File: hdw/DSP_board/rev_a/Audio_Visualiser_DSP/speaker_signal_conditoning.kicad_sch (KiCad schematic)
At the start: 6 parts, among them J1401 Left, T1401 Transformer_Audio

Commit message: assigned some footprints
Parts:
- R1401, R1402: footprint (none) -> Resistors_SMD:R_0805
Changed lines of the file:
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@@
 			)
 		)
-		(property "Footprint" ""
+		(property "Footprint" "Resistors_SMD:R_0805"
 			(at 132.08 63.5 0)
 			(hide yes)
@@
 				(font
 					(size 1.524 1.524)
+				)
+			)
+		)
+		(property "Sim.Type" ""
+			(at 132.08 63.5 90)
+			(hide yes)
+			(show_name no)
+			(do_not_autoplace no)
+			(effects
+				(font
+					(size 1.27 1.27)
 				)
 			)
@@
 			)
 		)
+		(property "Sim.Type" ""
+			(at 119.38 63.5 90)
+			(hide yes)
+			(show_name no)
+			(do_not_autoplace no)
+			(effects
+				(font
+					(size 1.27 1.27)
+				)
+			)
+		)
 		(pin "2"
 		)
@@
 			)
 		)
+		(property "Sim.Type" ""
+			(at 179.07 63.5 90)
+			(hide yes)
+			(show_name no)
+			(do_not_autoplace no)
+			(effects
+				(font
+					(size 1.27 1.27)
+				)
+			)
+		)
 		(pin "2"
 		)
@@
 			)
 		)
-		(property "Footprint" ""
+		(property "Footprint" "Resistors_SMD:R_0805"
 			(at 140.97 57.15 0)
 			(hide yes)
@@
 		)
 		(property "Digi-Key PN" ""
+			(at 140.97 57.15 0)
+			(hide yes)
+			(show_name no)
+			(do_not_autoplace no)
+			(effects
+				(font
+					(size 1.27 1.27)
+				)
+			)
+		)
+		(property "Sim.Type" ""
 			(at 140.97 57.15 0)
 			(hide yes)
@@
 		)
 		(property "Description" "Audio transformer"
+			(at 87.63 68.58 0)
+			(hide yes)
+			(show_name no)
+			(do_not_autoplace no)
+			(effects
+				(font
+					(size 1.27 1.27)
+				)
+			)
+		)
+		(property "Sim.Type" ""
 			(at 87.63 68.58 0)
 			(hide yes)
@@
 			(at 59.69 67.31 0)
 			(hide yes)
+			(show_name no)
+			(do_not_autoplace no)
+			(effects
+				(font
+					(size 1.27 1.27)
+				)
+			)
+		)
+		(property "Sim.Type" ""
+			(at 59.69 67.31 0)
+			(hide yes)

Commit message: assigned many digi-key part numbers
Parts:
- removed C1401: 2.2uF, Capacitors_SMD:C_0402, symbol Custom Library:C_Custom
- removed J1401: Left, symbol Connector:Screw_Terminal_01x02
- removed T1401: Transformer_Audio, symbol Device:Transformer_Audio
- D1401: Digi-Key PN (none) -> BAT54SWT1GOSCT-ND
- R1401, R1402: Digi-Key PN (none) -> 311-20.0KCRCT-ND; Wattage 1/4W -> 1/8W

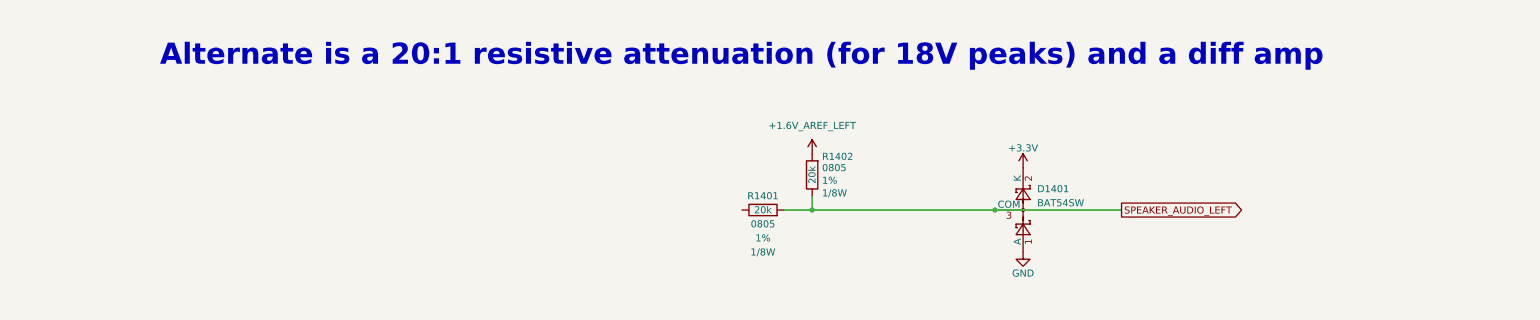
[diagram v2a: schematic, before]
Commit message: started speaker signal conditioning
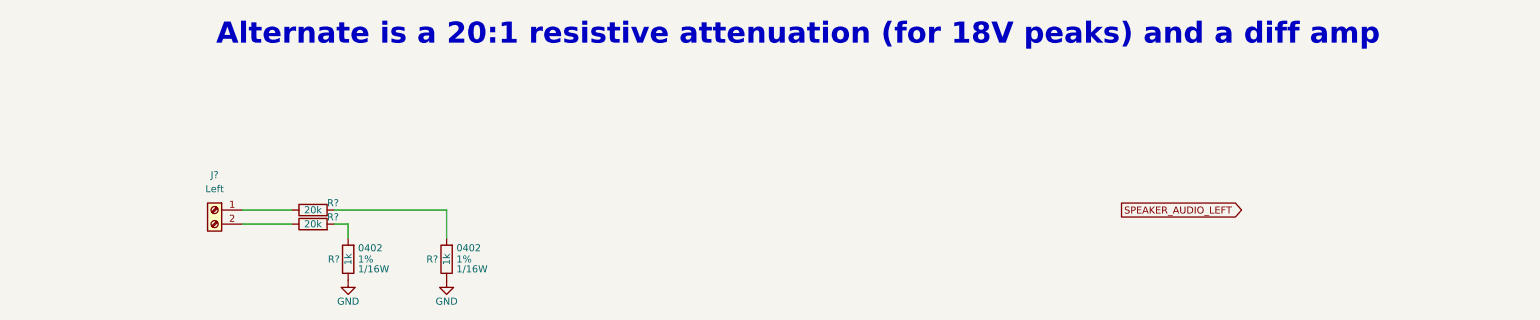
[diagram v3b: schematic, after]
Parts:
- removed D1401: BAT54SW, Package_TO_SOT_SMD:SOT-323_SC-70, symbol Diode:BAT54SW
- removed R1401: 20k, Resistors_SMD:R_0805, symbol Custom Library:R_Custom
- removed R1402: 20k, Resistors_SMD:R_0805, symbol Custom_Library:R_Custom
- added J?: Left, TerminalBlock_Phoenix:TerminalBlock_Phoenix_MKDS-1,5-2-5.08_1x02_P5.08mm_Horizontal, symbol Connector:Screw_Terminal_01x02
- added R? (x2): 1k, Resistors_SMD:R_0402, symbol Custom_Library:R_Custom
- added R? (x2): 20k, Resistors_SMD:R_0402, symbol Custom Library:R_Custom
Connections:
- net GND: now also R?.2, R?.2
- new net: R?.1, R?.1 (x2)
- new net: J?.1 (Pin_1), R?.2
- new net: J?.2 (Pin_2), R?.2

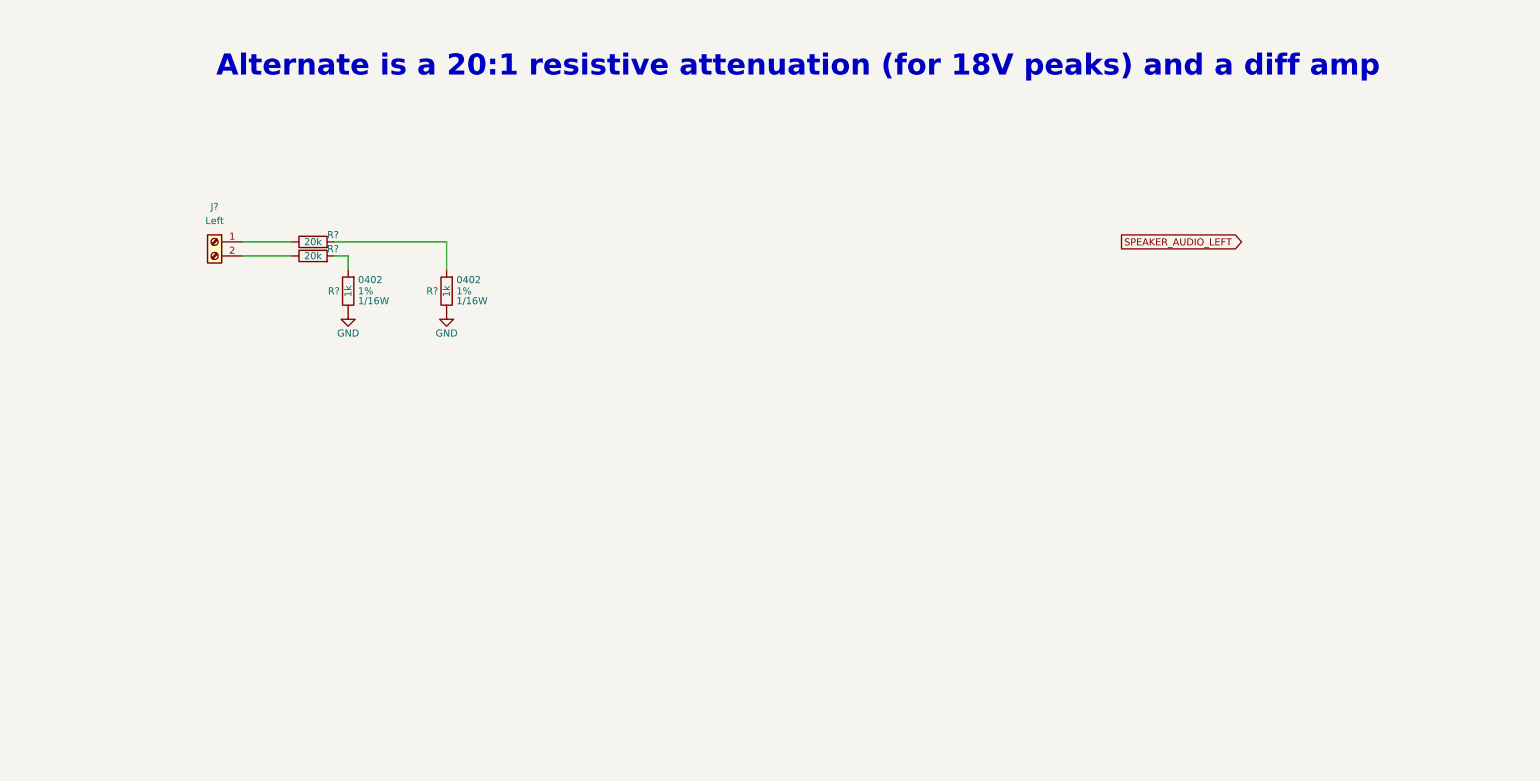
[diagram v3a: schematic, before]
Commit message: Added speaker signal path
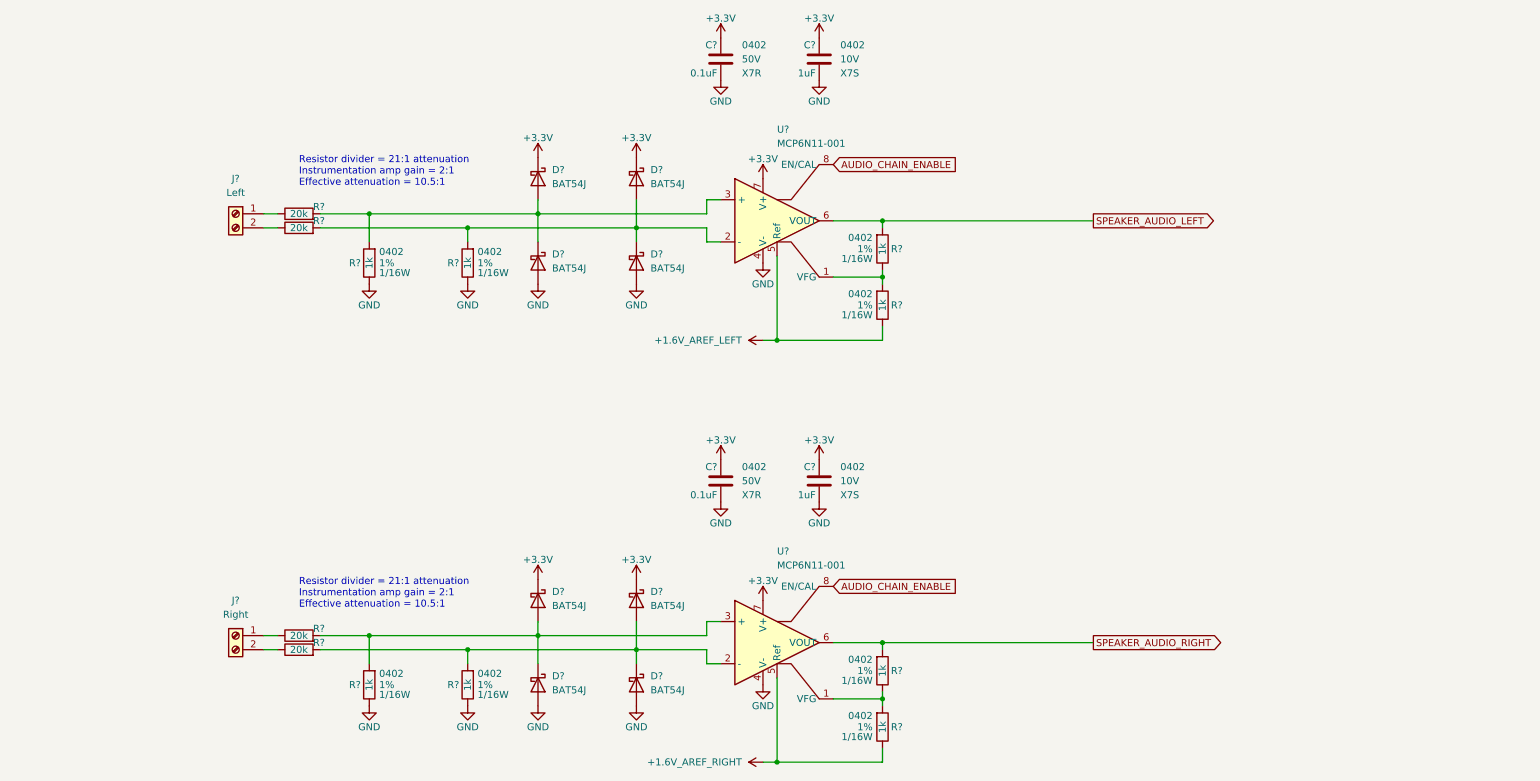
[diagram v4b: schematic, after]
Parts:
- added C? (x2): 0.1uF, Capacitors_SMD:C_0402, symbol Custom_Library:C_Custom
- added C? (x2): 1uF, Capacitors_SMD:C_0402, symbol Custom_Library:C_Custom
- added D? (x8): BAT54J, Diode_SMD:D_SOD-323F, symbol Diode:BAT54J
- added J?: Right, TerminalBlock_Phoenix:TerminalBlock_Phoenix_MKDS-1,5-2-5.08_1x02_P5.08mm_Horizontal, symbol Connector:Screw_Terminal_01x02
- added R? (x6): 1k, Resistors_SMD:R_0402, symbol Custom_Library:R_Custom
- added R? (x2): 20k, Resistors_SMD:R_0402, symbol Custom Library:R_Custom
- added U? (x2): MCP6N11-001, Housings_DFN_QFN:DFN-8-1EP_2x3mm_Pitch0.5mm, symbol MCP6N11:MCP6N11-001
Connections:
- net GND: now also C?.2, C?.2, C?.2, C?.2, D?.2 (A), D?.2 (A), D?.2 (A), D?.2 (A), R?.2, R?.2, U?.4 (V-), U?.4 (V-), U?.9 (EP), U?.9 (EP)
- net SPEAKER_AUDIO_LEFT: now also R?.1, U?.6 (VOUT)
- net at R?.1: now also R?.1, D?.1 (K), D?.2 (A), U?.2 (-); no longer R?.1
- net at R?.1: now also R?.1, D?.1 (K), D?.2 (A), U?.3 (+); no longer R?.1
- new net: R?.1, R?.2, U?.1 (VFG) (x2)
- new net: D?.1 (K), D?.2 (A), R?.1, R?.1, U?.3 (+)
- new net: J?.1 (Pin_1), R?.2
- new net: J?.2 (Pin_2), R?.2
- new net: D?.1 (K), D?.2 (A), R?.1, R?.1, U?.2 (-)
- new net +1.6V_AREF_LEFT: R?.2, U?.5 (Ref)
- new net +1.6V_AREF_RIGHT: R?.2, U?.5 (Ref)
- new net +3.3V: C?.1, C?.1, C?.1, C?.1, D?.1 (K), D?.1 (K), D?.1 (K), D?.1 (K), U?.7 (V+), U?.7 (V+)
- new net AUDIO_CHAIN_ENABLE: U?.8 (EN/CAL), U?.8 (EN/CAL)
- new net SPEAKER_AUDIO_RIGHT: R?.1, U?.6 (VOUT)
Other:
- note added: "Resistor divider = 21:1 attenuation Instrumentation amp gain = 2:1 Effective attenuation = 10.5:1"
- note removed: "Alternate is a 20:1 resistive attenuation (for 18V peaks) and a diff amp"
- moved on the sheet: J?, R?

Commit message: add simulation data for speaker input path
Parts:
- gave numbers to parts that had none: 28

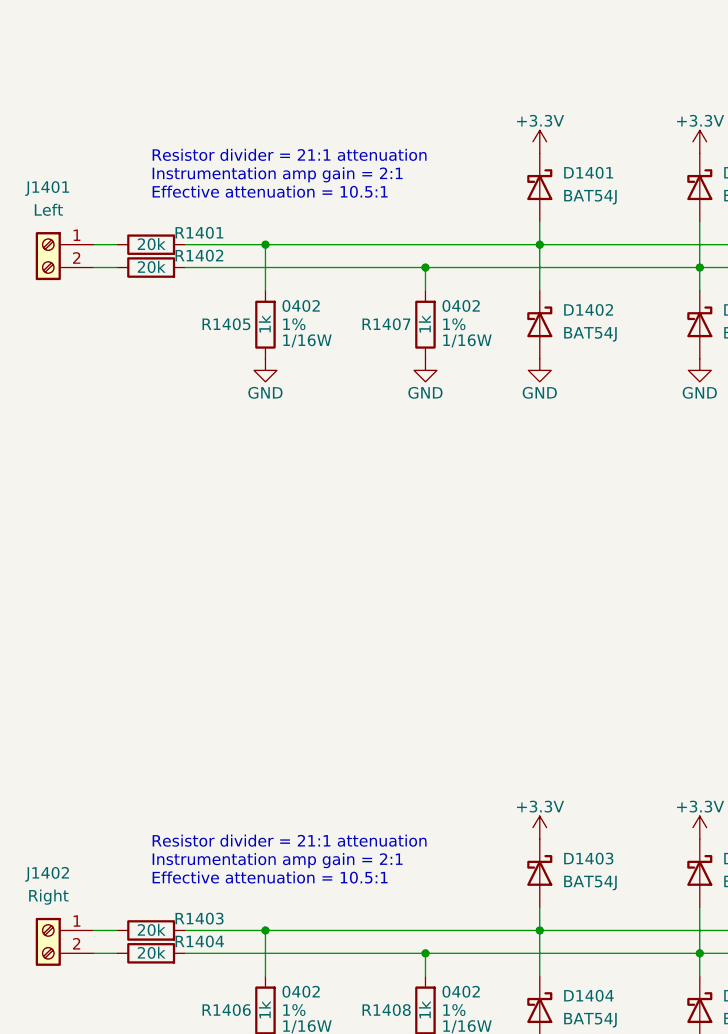
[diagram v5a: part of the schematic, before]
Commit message: Change RCA input signal paths to use instrumentation amp instead of AC coupling cap
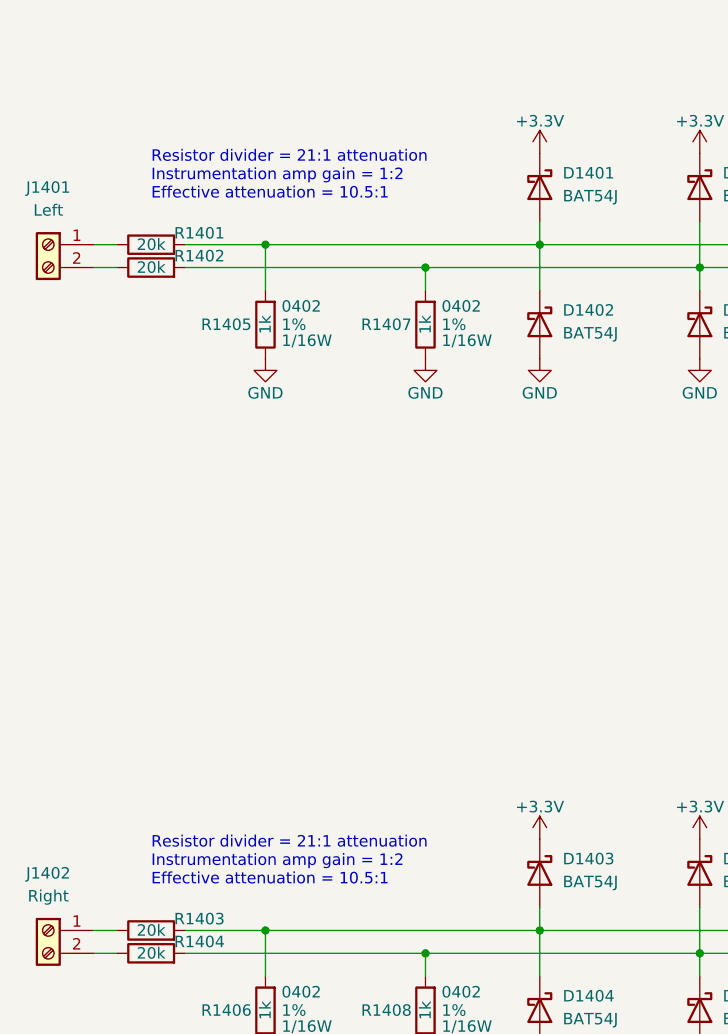
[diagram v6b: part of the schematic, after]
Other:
- note added: "Resistor divider = 21:1 attenuation Instrumentation amp gain = 1:2 Effective attenuation = 10.5:1"
- note removed: "Resistor divider = 21:1 attenuation Instrumentation amp gain = 2:1 Effective attenuation = 10.5:1"
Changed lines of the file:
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@@
 		(date "2023-12-25")
 	)
-	(text "Resistor divider = 21:1 attenuation\nInstrumentation amp gain = 2:1\nEffective attenuation = 10.5:1"
+	(text "Resistor divider = 21:1 attenuation\nInstrumentation amp gain = 1:2\nEffective attenuation = 10.5:1"
 		(exclude_from_sim no)
 		(at 48.26 50.8 0)
@@
 		)
 	)
-	(text "Resistor divider = 21:1 attenuation\nInstrumentation amp gain = 2:1\nEffective attenuation = 10.5:1"
+	(text "Resistor divider = 21:1 attenuation\nInstrumentation amp gain = 1:2\nEffective attenuation = 10.5:1"
 		(exclude_from_sim no)
 		(at 48.26 127 0)

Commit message: Revert "Change RCA input signal paths to use instrumentation amp instead of AC coupling cap"
This reverts commit f4dee5b3753607e11cfd8388ae674b9233847bc3.
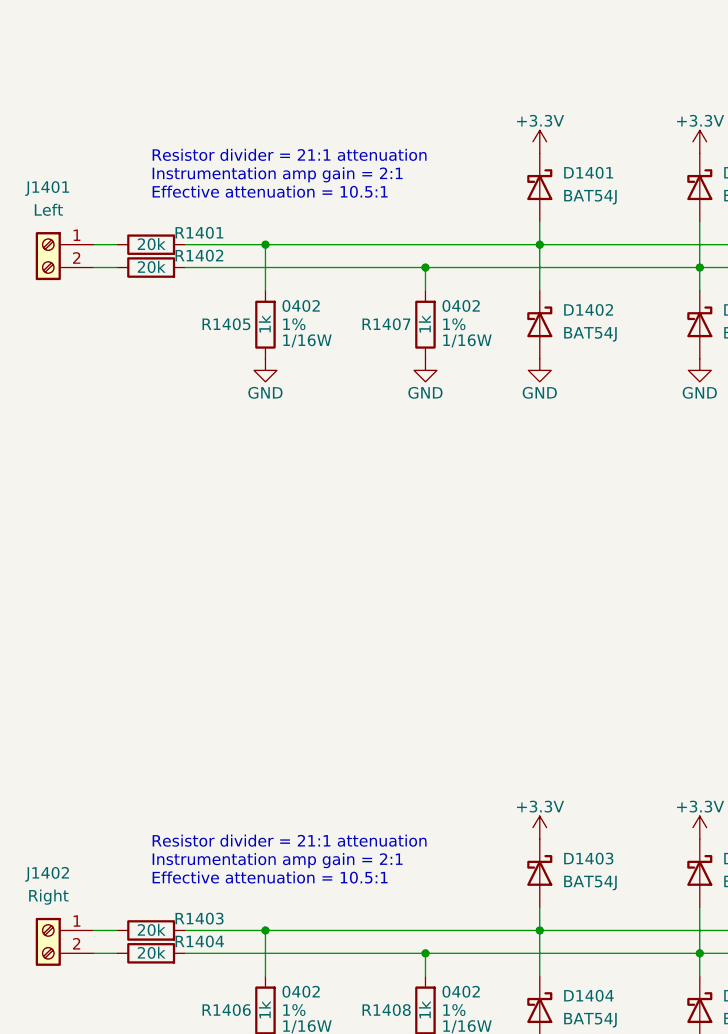
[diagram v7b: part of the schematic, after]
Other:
- note added: "Resistor divider = 21:1 attenuation Instrumentation amp gain = 2:1 Effective attenuation = 10.5:1"
- note removed: "Resistor divider = 21:1 attenuation Instrumentation amp gain = 1:2 Effective attenuation = 10.5:1"
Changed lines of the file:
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@@
 		(date "2023-12-25")
 	)
-	(text "Resistor divider = 21:1 attenuation\nInstrumentation amp gain = 1:2\nEffective attenuation = 10.5:1"
+	(text "Resistor divider = 21:1 attenuation\nInstrumentation amp gain = 2:1\nEffective attenuation = 10.5:1"
 		(exclude_from_sim no)
 		(at 48.26 50.8 0)
@@
 		)
 	)
-	(text "Resistor divider = 21:1 attenuation\nInstrumentation amp gain = 1:2\nEffective attenuation = 10.5:1"
+	(text "Resistor divider = 21:1 attenuation\nInstrumentation amp gain = 2:1\nEffective attenuation = 10.5:1"
 		(exclude_from_sim no)
 		(at 48.26 127 0)
